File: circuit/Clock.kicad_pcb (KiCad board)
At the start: 2 copper layers, 81.3 x 33.7 mm, 17 parts, among them U2 Max98357

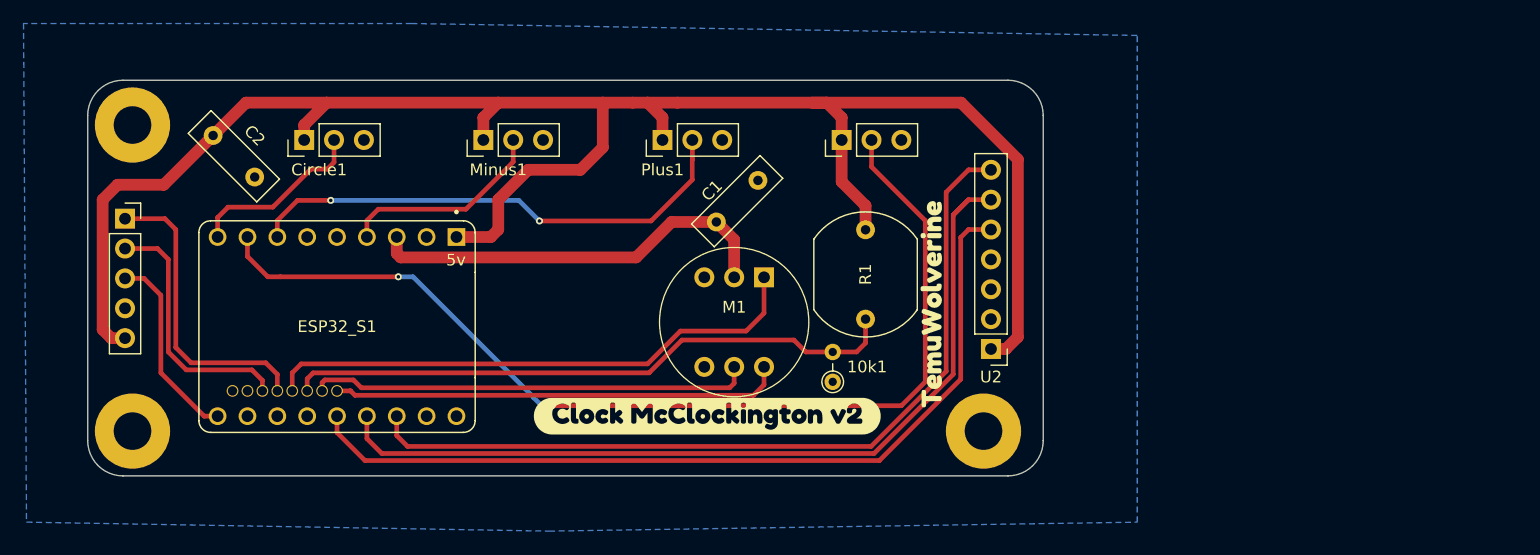
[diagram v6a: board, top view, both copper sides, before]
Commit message: switched to mom-switches rather than ttp223 capacitive sensors
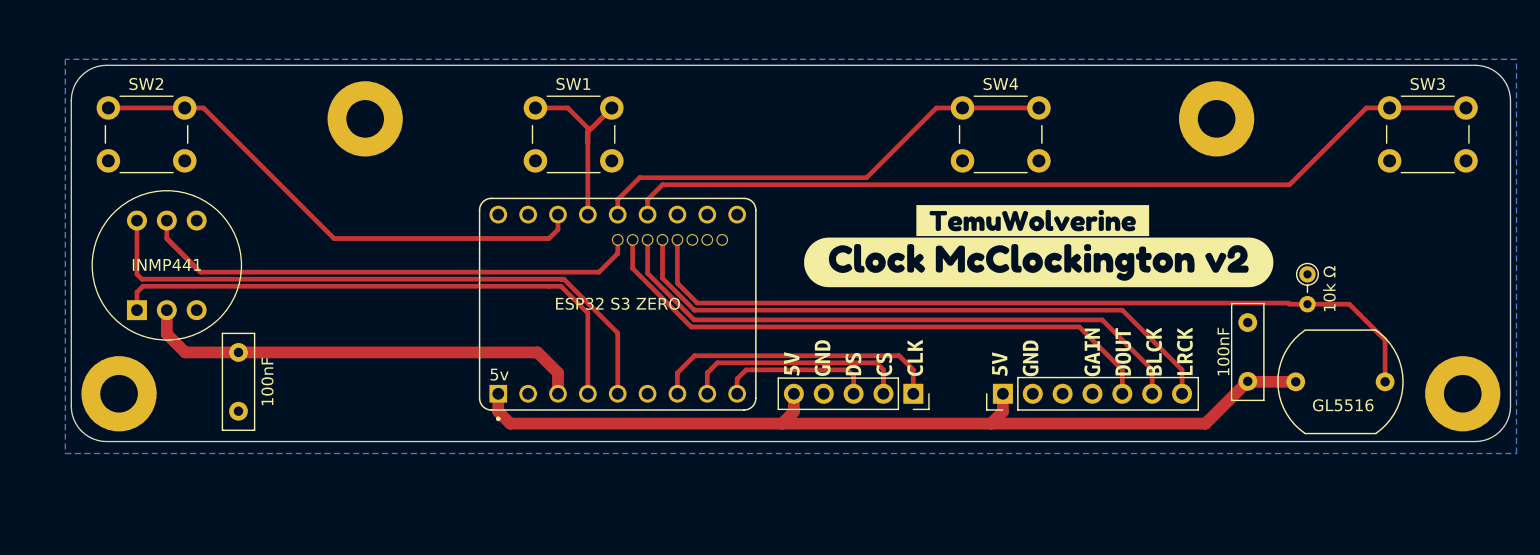
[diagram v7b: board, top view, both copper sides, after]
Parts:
- removed 10k1: R, Resistor_THT:R_Axial_DIN0204_L3.6mm_D1.6mm_P2.54mm_Vertical
- removed C1, C2: 100nF, Capacitor_THT:C_Disc_D8.0mm_W2.5mm_P5.00mm
- removed Circle1, Minus1, Plus1, Triangle1: TPP223, Connector_PinHeader_2.54mm:PinHeader_1x03_P2.54mm_Vertical
- removed ESP32_S1: ~, PaulsCoolKicadLibrary:MODULE_ESP32-S3-ZERO
- removed M1: ~, PaulsCoolKicadLibrary:INMP441
- removed R1: LDR03, OptoDevice:R_LDR_10x8.5mm_P7.6mm_Vertical
- removed kibuzzard-696B2912: G***, kibuzzard-696B2912
- removed kibuzzard-69B23704: G***, kibuzzard-69B23704
- added 100nF: 100nF, Capacitor_THT:C_Disc_D8.0mm_W2.5mm_P5.00mm, F.Cu at (129.0, 112.0)
- added 100nF: 100nF, Capacitor_THT:C_Disc_D8.0mm_W2.5mm_P5.00mm, F.Cu at (214.8, 114.4)
- added 10k Ω: R, Resistor_THT:R_Axial_DIN0204_L3.6mm_D1.6mm_P2.54mm_Vertical, F.Cu at (219.9, 105.3)
- added ESP32 S3 ZERO: ~, PaulsCoolKicadLibrary:MODULE_ESP32-S3-ZERO, F.Cu at (161.2, 107.9)
- added GL5516 : LDR03, OptoDevice:R_LDR_10x8.5mm_P7.6mm_Vertical, F.Cu at (226.5, 114.5)
- added H4: MountingHole_Pad, MountingHole:MountingHole_3.2mm_M3_Pad, F.Cu at (139.7, 92.1)
- added INMP441: ~, PaulsCoolKicadLibrary:INMP441, F.Cu at (120.3, 108.4)
- added SW1: SW_Push, Button_Switch_THT:SW_PUSH_6mm_H5mm, F.Cu at (154.2, 91.2)
- added SW2: SW_Push, Button_Switch_THT:SW_PUSH_6mm_H5mm, F.Cu at (117.9, 91.2)
- added SW3: SW_Push, Button_Switch_THT:SW_PUSH_6mm_H5mm, F.Cu at (226.9, 91.2)
- added SW4: SW_Push, Button_Switch_THT:SW_PUSH_6mm_H5mm, F.Cu at (190.5, 91.2)
- added kibuzzard-69B4FF18: G***, kibuzzard-69B4FF18, F.Cu at (197.0, 104.3)
- added kibuzzard-69B4FF3C: G***, kibuzzard-69B4FF3C, F.Cu at (196.5, 100.8)
- added kibuzzard-69B50323: G***, kibuzzard-69B50323, F.Cu at (181.3, 112.4)
- added kibuzzard-69B50368: G***, kibuzzard-69B50368, F.Cu at (201.6, 111.9)
- moved H2 113.2 mm to (233.1, 115.5)
- moved H1 92.2 mm to (212.2, 92.1)
- moved H3 73.6 mm to (118.8, 115.5)
- moved Display1 68.7 mm to (186.4, 115.5), turned to -90 degrees
- moved U2 3.94 mm to (194.0, 115.5), turned to 90 degrees
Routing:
- net triangle: track 87.9 -> 0.00 mm, vias 2 -> 0
- net +5V: track 160.1 -> 77.2 mm
- net btnFour: track 0.00 -> 74.1 mm
- net btnOne: track 0.00 -> 44.4 mm
- net PlusSignal: track 43.0 -> 0.00 mm, vias 2 -> 0
- net btnThree: track 0.00 -> 40.3 mm
- net SPK_DOUT: track 73.2 -> 49.7 mm
- net BLCK: track 74.2 -> 51.2 mm
- net btnTwo: track 0.00 -> 18.8 mm
- net LRCK: track 71.3 -> 52.7 mm
- net MinusSignal: track 17.8 -> 0.00 mm
- net PhotoresistorSignal: track 52.7 -> 69.4 mm
- net circle: track 15.4 -> 0.00 mm
- net SCK: track 38.4 -> 52.7 mm
- net WS: track 37.7 -> 46.5 mm
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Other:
- board size 81.3 x 33.7 mm -> 122.4 x 32 mm

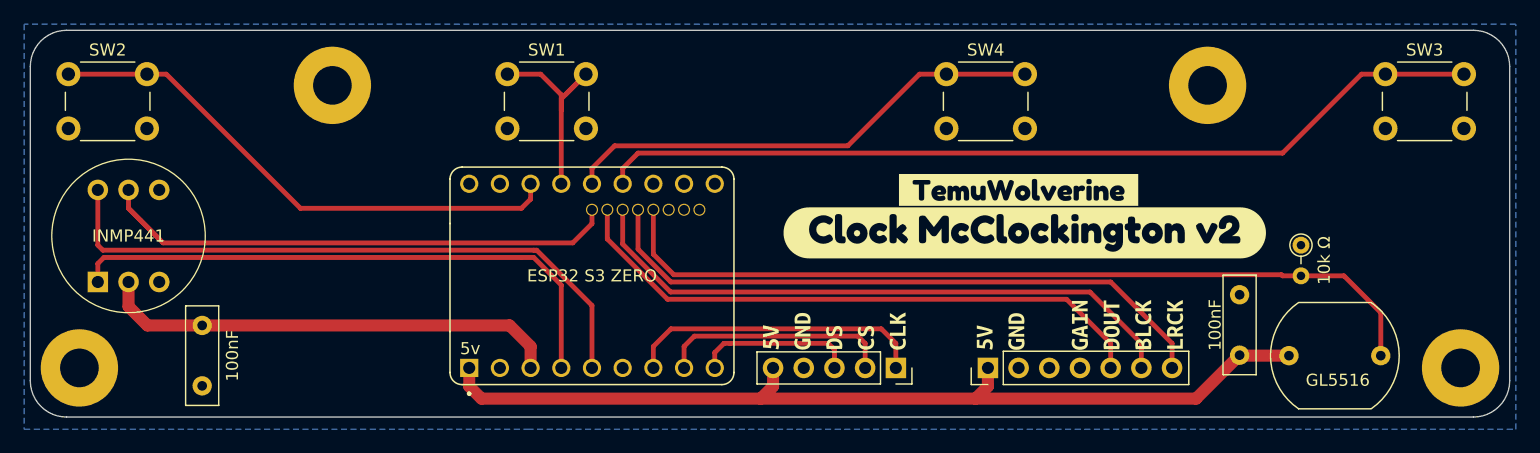
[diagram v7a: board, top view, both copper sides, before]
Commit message: fully functional based on breadboard prototype
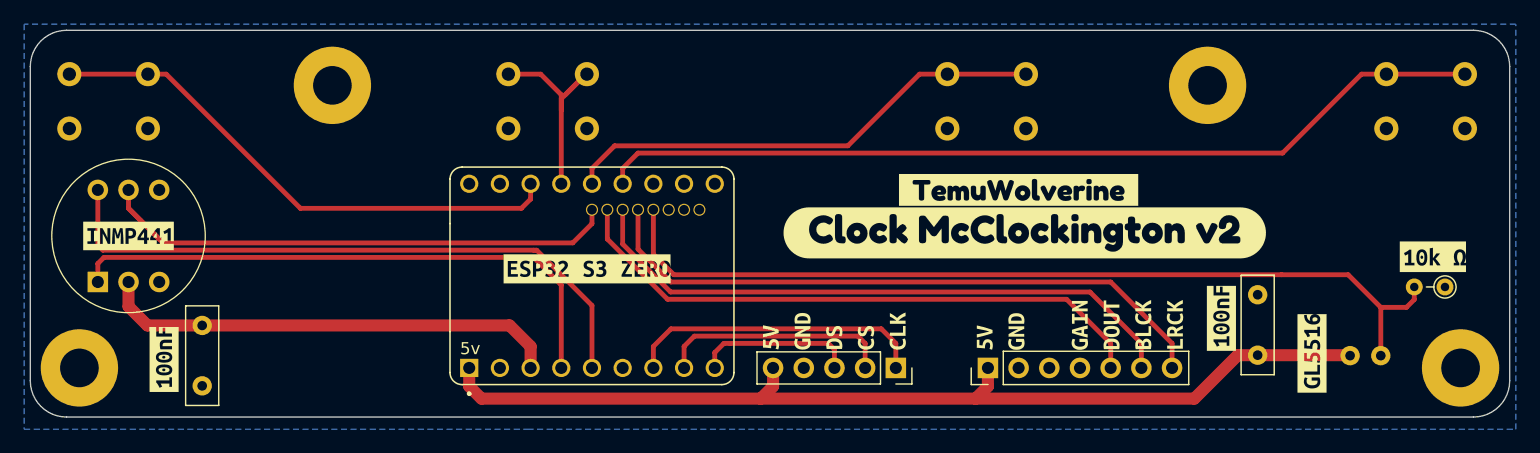
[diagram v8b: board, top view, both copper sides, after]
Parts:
- added kibuzzard-69B74ACD: G***, kibuzzard-69B74ACD, F.Cu at (160.8, 107.3)
- added kibuzzard-69B74AE8: G***, kibuzzard-69B74AE8, F.Cu at (122.9, 104.6)
- added kibuzzard-69B74AF7: G***, kibuzzard-69B74AF7, F.Cu at (220.8, 114.3)
- added kibuzzard-69B74B07: G***, kibuzzard-69B74B07, F.Cu at (230.8, 106.3)
- added kibuzzard-69B74B24: G***, kibuzzard-69B74B24, F.Cu at (213.3, 111.4)
- added kibuzzard-69B74B24: G***, kibuzzard-69B74B24, F.Cu at (125.8, 114.8)
- 10k1: renamed from 10k Ω
- ESP32_S1: renamed from ESP32 S3 ZERO
- R1: renamed from GL5516 ; footprint OptoDevice:R_LDR_10x8.5mm_P7.6mm_Vertical -> OptoDevice:R_LDR_4.9x4.2mm_P2.54mm_Vertical; moved to B.Cu
- SW1, SW2, SW3, SW4: moved to B.Cu
- moved 10k1 12.4 mm to (231.8, 108.8), turned to 180 degrees
- moved SW4 6.58 mm to (197.1, 91.2), turned to 180 degrees
- moved SW2 6.58 mm to (124.5, 91.2), turned to 180 degrees
- moved SW1 6.58 mm to (160.8, 91.2), turned to 180 degrees
- moved SW3 6.58 mm to (233.4, 91.2), turned to 180 degrees
- moved C2 1.50 mm to (216.3, 114.4)
- renumbered 100nF to C1, 100nF to C2, INMP441 to M1
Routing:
- net +5V: track 77.2 -> 82.3 mm
- net PhotoresistorSignal: track 69.4 -> 73.8 mm
